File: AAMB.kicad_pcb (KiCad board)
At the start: 4 copper layers, 159.4 x 76.6 mm, 192 parts, among them J1 Screw_Terminal_01x04, J2 PJRAS4X2U01X, J3 SPKR L, J4 SPKR R, J5 Screw_Terminal_01x03, J6 Screw_Terminal_01x03, J7 Screw_Terminal_01x04, K1 G5LE-1, K2 G5LE-1, Q1 BC546, Q2 BC556, Q201 BC546, Q202 BC546, Q203 BC546, Q204 BD140, Q205 BD139, Q206 BD140, Q207 MJL21193, Q208 MJL21194, Q209 BC546, Q3 BC546, Q301 BC546, Q302 BC546, Q303 BC546, Q304 BD140, Q305 BD139, Q306 BD140, Q307 MJL21193, Q308 MJL21194, Q309 BC546, Q4 BD140, U1 TL072, U2 NE5532, U3 NE5532, U4 THAT2180, U5 DG509BEQ-T1-E3, U6 CD4071B

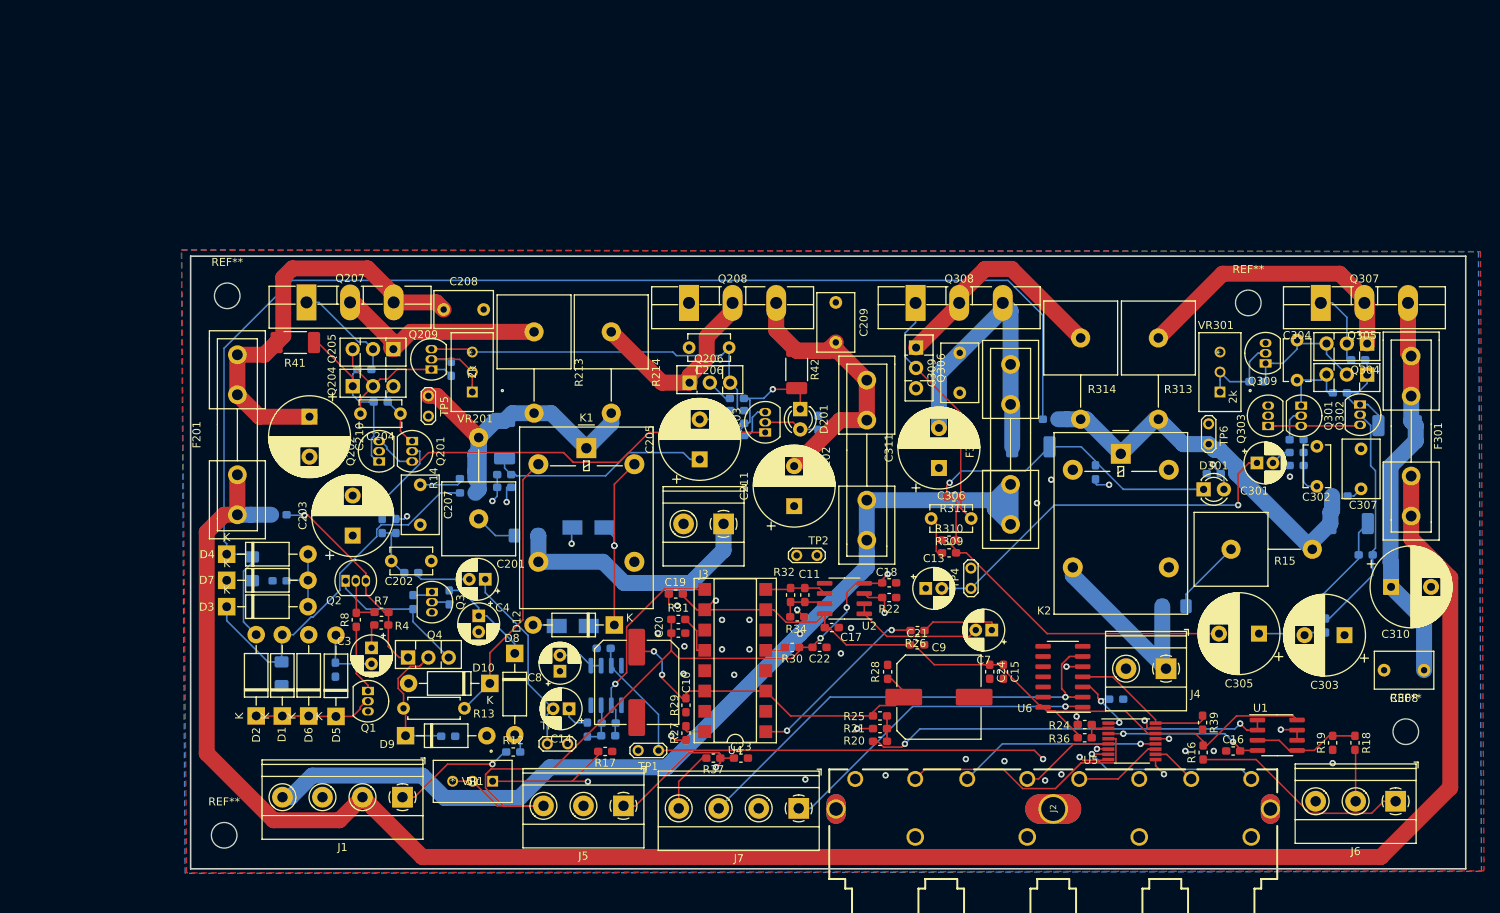
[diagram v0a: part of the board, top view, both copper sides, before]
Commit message: Lots of part changes to SMD devices. Adding MPN, MFG to all parts for BOM export.
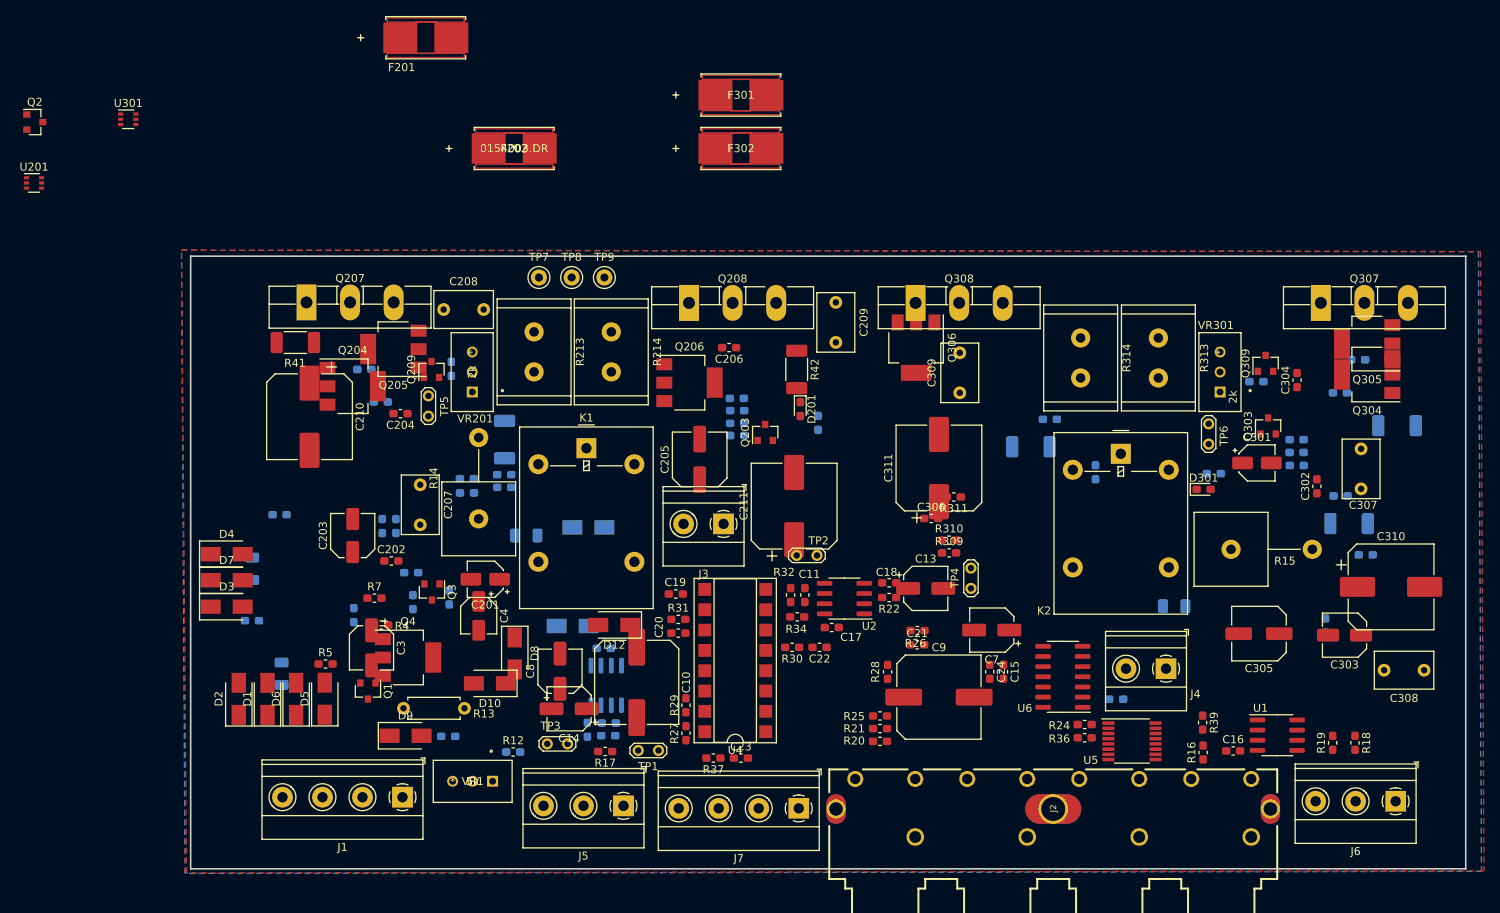
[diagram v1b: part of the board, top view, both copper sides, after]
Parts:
- removed Q201, Q202, Q301, Q302: BC546, Package_TO_SOT_THT:TO-92_Inline
- removed REF** (x4): MountingHole_3.2mm_M3, MountingHole:MountingHole_3.2mm_M3
- added TP7: 5002, digikey-footprints:Test_Point_D1.02mm, F.Cu at (102.6, 62.4)
- added TP8: 5000, digikey-footprints:Test_Point_D1.02mm, F.Cu at (106.7, 62.4)
- added TP9: 5001, digikey-footprints:Test_Point_D1.02mm, F.Cu at (110.8, 62.4)
- added U201: BC846BDW1T1G, Package_TO_SOT_SMD:SOT-363_SC-70-6, F.Cu at (39.5, 50.5)
- added U301: BC846BDW1T1G, Package_TO_SOT_SMD:SOT-363_SC-70-6, F.Cu at (51.3, 42.6)
- C1, C2, C5, C6: footprint Capacitor_SMD:C_1206_3216Metric_Pad1.42x1.75mm_HandSolder -> Capacitor_SMD:C_1206_3216Metric
- C13, C14, C3, C7, C8: footprint Capacitor_THT:CP_Radial_D5.0mm_P2.00mm -> Capacitor_SMD:CP_Elec_5x3
- C201, C301, C4: footprint Capacitor_THT:CP_Radial_D5.0mm_P2.00mm -> Capacitor_SMD:CP_Elec_4x5.4
- C202, C204, C206, C302, C304, C306: footprint Capacitor_THT:C_Disc_D5.1mm_W3.2mm_P5.00mm -> Capacitor_SMD:C_0603_1608Metric_Pad1.05x0.95mm_HandSolder
- C203, C303: footprint Capacitor_THT:CP_Radial_D10.0mm_P5.00mm -> Capacitor_SMD:C_Elec_5x5.4
- C205, C305: footprint Capacitor_THT:CP_Radial_D10.0mm_P5.00mm -> Capacitor_SMD:C_Elec_6.3x7.7
- C210, C211, C310, C311: footprint Capacitor_THT:CP_Radial_D10.0mm_P5.00mm -> Capacitor_SMD:CP_Elec_10x10.5
- D1, D10, D12, D2, D3, D4, D5, D6, D7, D8, D9: value 1N4004 -> S1G; footprint Diode_THT:D_DO-41_SOD81_P10.16mm_Horizontal -> Diode_SMD:D_SMA
- D201, D301: footprint LED_THT:LED_D3.0mm -> LED_SMD:LED_0603_1608Metric_Pad1.05x0.95mm_HandSolder
- F201, F202, F301, F302: value 3A -> 0154003.DR; footprint Fuseholders:Fuseholder5x20_horiz_open_inline_Type-I -> Fuse:0154003.DR
- J3: value SPKR L -> SPKR
- J4: value SPKR R -> SPKR
- Q1, Q203, Q209, Q3, Q303, Q309: value BC546 -> BC846; footprint Package_TO_SOT_THT:TO-92_Inline -> Package_TO_SOT_SMD:SOT-23
- Q2: value BC556 -> BC856; footprint Package_TO_SOT_THT:TO-92_Inline -> Package_TO_SOT_SMD:SOT-23
- Q204, Q206, Q304, Q306, Q4: value BD140 -> BCP53; footprint Package_TO_SOT_THT:TO-126-3_Vertical -> Package_TO_SOT_SMD:SOT-223
- Q205, Q305: value BD139 -> BCP56; footprint Package_TO_SOT_THT:TO-126-3_Vertical -> Package_TO_SOT_SMD:SOT-223
- R213, R214, R313, R314: value 15m -> 330m; footprint Resistor_THT:R_Axial_Power_L25.0mm_W9.0mm_P10.16mm_Vertical -> Resistor_THT:R_Radial_Power_L13.0mm_W9.0mm_P5.00mm
- R5: moved to F.Cu
- R8: moved to B.Cu
- TP1: value post_sw_pre_vol_L -> TP
- TP2: value post_sw_pre_vol_R -> TP
- TP3: value post_vol_pre_amp_L -> TP
- TP4: value post_vol_pre_amp_R -> TP
- TP5: value post_amp_pre_rly_L -> TP
- TP6: value post_amp_pre_rly_R -> TP
- moved F301 98.9 mm to (127.8, 39.5), turned to 0 degrees
- moved Q2 69.3 mm to (39.6, 42.9)
- moved F202 65.9 mm to (99.5, 46.2), turned to 0 degrees
- moved F201 64.1 mm to (88.4, 32.4), turned to 0 degrees
- moved F302 57.8 mm to (127.8, 46.2), turned to 0 degrees
- moved R6 6.07 mm to (66.7, 105.3), turned to 180 degrees
- moved D2 3.05 mm to (65.1, 115.0)
- moved D1 2.84 mm to (68.7, 115.0)
- moved D6 2.67 mm to (72.2, 115.0)
- moved D5 2.62 mm to (75.8, 115.0)
- moved R7 1.98 mm to (82.0, 102.4)
- moved R5 1.43 mm to (75.9, 110.7), turned to 0 degrees
- moved R8 0.66 mm to (79.5, 104.6)
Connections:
- F201 pad 1: +35V -> /audio_pwr_L/P35_fused_L
- F201 pad 2: /audio_pwr_L/P35_fused_L -> +35V
- F202 pad 1: -35V -> /audio_pwr_L/N35_fused_L
- F202 pad 2: /audio_pwr_L/N35_fused_L -> -35V
- F301 pad 1: +35V -> /audio_pwr_R/P35_fused_R
- F301 pad 2: /audio_pwr_R/P35_fused_R -> +35V
- F302 pad 1: -35V -> /audio_pwr_R/N35_fused_R
- F302 pad 2: /audio_pwr_R/N35_fused_R -> -35V
- Q4 pad 3: Net-(Q2-Pad1) -> Net-(Q2-Pad2)
- R7 pad 1: Net-(Q2-Pad2) -> Net-(Q2-Pad1)
- R8 pad 2: Net-(Q2-Pad2) -> Net-(Q2-Pad1)
- R9 pad 2: Net-(Q2-Pad1) -> Net-(Q2-Pad2)
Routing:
- net +35V: track 249.4 -> 0.00 mm
- net Net-(C2-Pad1): track 160.7 -> 0.00 mm
- net -12V: track 148.8 -> 0.00 mm, vias 5 -> 0
- net +12V: track 135.5 -> 0.00 mm, vias 2 -> 0
- net -35V: track 123.3 -> 0.00 mm, vias 1 -> 0
- net /volume/vol_pot_3: track 112.3 -> 0.00 mm, vias 1 -> 0
- net /short_protection_muting/RLY_-L_+R: track 81.1 -> 0.00 mm, vias 2 -> 0
- net /pre_vol_audio_L: track 72.3 -> 0.00 mm, vias 2 -> 0
- net Net-(C306-Pad1): track 68.4 -> 0.00 mm
- net /pre_vol_audio_R: track 61.4 -> 0.00 mm, vias 2 -> 0
- net /input_select/input_sw_3: track 59.6 -> 0.00 mm, vias 1 -> 0
- net Net-(R21-Pad2): track 59.2 -> 0.00 mm, vias 2 -> 0
- net /audio_pwr_L/P35_fused_L: track 52.4 -> 0.00 mm
- net Net-(Q203-Pad1): track 51.9 -> 0.00 mm
- net Net-(R20-Pad2): track 51.2 -> 0.00 mm, vias 2 -> 0
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
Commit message: Layout startover, sorting, some routing. Removed redundant fuses. BOM export.
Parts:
- removed F201, F202, F301, F302: 0154003.DR, Fuse:0154003.DR
- added F1: Fuse_Small, Resistor_SMD:R_1206_3216Metric_Pad1.42x1.75mm_HandSolder, F.Cu at (44.0, 182.0)
- added F2: Fuse_Small, Resistor_SMD:R_1206_3216Metric_Pad1.42x1.75mm_HandSolder, F.Cu at (34.0, 181.7)
- added TP10: 5002, digikey-footprints:Test_Point_D1.02mm, F.Cu at (379.7, 65.5)
- added TP11: 5000, digikey-footprints:Test_Point_D1.02mm, F.Cu at (383.8, 65.5)
- added TP12: 5001, digikey-footprints:Test_Point_D1.02mm, F.Cu at (387.9, 65.5)
- C1, C12, C2, C6, D11, D13, R1, R10, R11, R12, R2, R23, R3, R33, R35, R6, R8, R9, U3: moved to F.Cu
- R13: footprint Resistor_THT:R_Axial_DIN0207_L6.3mm_D2.5mm_P7.62mm_Horizontal -> Resistor_SMD:R_2512_6332Metric
- R14, R15: footprint Resistor_THT:R_Axial_Power_L25.0mm_W9.0mm_P10.16mm_Vertical -> Resistor_THT:R_Axial_DIN0918_L18.0mm_D9.0mm_P7.62mm_Vertical
- R24, R36, R39: moved to B.Cu
- moved U301 372.9 mm to (421.0, 91.5)
- moved R12 225.9 mm to (148.4, -98.8)
- moved Q4 211.2 mm to (139.7, -94.5)
- moved J3 210.9 mm to (156.7, -115.4)
- moved R6 209.9 mm to (130.2, -94.8), turned to 90 degrees
- moved D10 208.0 mm to (162.2, -84.3)
- moved K1 207.2 mm to (135.7, -121.8)
- moved C309 207.1 mm to (362.3, 78.8)
- moved Q308 207.1 mm to (356.8, 67.6)
- moved R306 207.1 mm to (409.8, 78.8)
- moved R308 207.1 mm to (394.1, 88.9)
- moved R312 207.1 mm to (412.1, 74.7)
- moved R314 207.1 mm to (377.4, 72.0)
- moved R316 207.1 mm to (399.4, 77.4)
- moved R44 207.1 mm to (417.0, 82.9)
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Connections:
- C208 pad 1: /audio_pwr_L/P35_fused_L -> +35V
- C209 pad 2: /audio_pwr_L/N35_fused_L -> -35V
- C210 pad 1: /audio_pwr_L/P35_fused_L -> +35V
- C211 pad 2: /audio_pwr_L/N35_fused_L -> -35V
- C308 pad 1: /audio_pwr_R/P35_fused_R -> +35V
- C309 pad 2: /audio_pwr_R/N35_fused_R -> -35V
- C310 pad 1: /audio_pwr_R/P35_fused_R -> +35V
- C311 pad 2: /audio_pwr_R/N35_fused_R -> -35V
- J1 pad 2: +35V -> Net-(F1-Pad1)
- J1 pad 4: -35V -> Net-(F2-Pad1)
- Q207 pad 3: /audio_pwr_L/P35_fused_L -> +35V
- Q208 pad 3: /audio_pwr_L/N35_fused_L -> -35V
- Q307 pad 3: /audio_pwr_R/P35_fused_R -> +35V
- Q308 pad 3: /audio_pwr_R/N35_fused_R -> -35V
- R41 pad 1: /audio_pwr_L/P35_fused_L -> +35V
- R42 pad 1: /audio_pwr_L/N35_fused_L -> -35V
- R44 pad 1: /audio_pwr_R/P35_fused_R -> +35V
- R45 pad 1: /audio_pwr_R/N35_fused_R -> -35V
- U4 pad 13: Net-(U4-Pad13) -> (no net)
- U4 pad 4: Net-(U4-Pad4) -> (no net)
- U6 pad 10: Net-(U6-Pad10) -> (no net)
- U6 pad 11: Net-(U6-Pad11) -> (no net)
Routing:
- net /input_select/IN4_L: track 0.00 -> 29.4 mm
- net /input_select/IN1_R: track 0.00 -> 27.4 mm
- net /input_select/IN1_L: track 0.00 -> 25.9 mm, vias 0 -> 1
- net -12V: track 0.00 -> 21.2 mm, vias 0 -> 1
- net /input_select/IN4_R: track 0.00 -> 20.6 mm
- net +12V: track 0.00 -> 19.7 mm, vias 0 -> 1
- net /input_select/input_sw_1: track 0.00 -> 16.9 mm
- net Net-(R39-Pad1): track 0.00 -> 16.1 mm, vias 0 -> 2
- net /input_select/input_sw_3: track 0.00 -> 16.0 mm
- net Net-(R38-Pad1): track 0.00 -> 15.3 mm, vias 0 -> 2
- net /input_select/IN2_R: track 0.00 -> 15.0 mm
- net /input_select/IN3_L: track 0.00 -> 14.4 mm
- net GND: track 0.00 -> 14.3 mm, vias 0 -> 15
- net /input_select/input_sw_com: track 0.00 -> 13.6 mm
- net /input_select/IN3_R: track 0.00 -> 9.74 mm
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- removed copper zone on In1.Cu, net GND
- removed copper zone on In2.Cu, net GND
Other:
- board outline removed
- copper layers 4 -> 2

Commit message: Layout progress. Added two missing decoupling caps.
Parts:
- added C25: 0.1u, Capacitor_SMD:C_0603_1608Metric_Pad1.05x0.95mm_HandSolder, F.Cu at (84.5, 257.7)
- added C26: 0.1u, Capacitor_SMD:C_0603_1608Metric_Pad1.05x0.95mm_HandSolder, B.Cu at (84.1, 270.3)
- C15, C18, C19, C21, R17, R23: moved to B.Cu
- moved C19 223.5 mm to (89.8, 262.7), turned to 270 degrees
- moved C20 217.6 mm to (85.4, 263.8), turned to 270 degrees
- moved C22 212.9 mm to (97.7, 263.7), turned to 270 degrees
- moved C9 173.2 mm to (104.2, 275.8)
- moved C7 167.0 mm to (103.3, 266.5)
- moved C15 166.2 mm to (80.4, 283.7), turned to 90 degrees
- moved C21 162.8 mm to (93.4, 262.7), turned to 270 degrees
- moved R28 162.8 mm to (97.9, 272.7)
- moved C8 162.6 mm to (81.5, 273.6), turned to 90 degrees
- moved U1 162.0 mm to (81.0, 283.8), turned to 180 degrees
- moved R26 160.2 mm to (98.7, 269.6)
- moved C13 159.3 mm to (110.2, 266.3), turned to 270 degrees
- moved R25 158.9 mm to (75.4, 281.6), turned to 0 degrees
- moved R20 158.8 mm to (75.4, 283.1), turned to 0 degrees
- moved R21 158.8 mm to (75.5, 284.7), turned to 0 degrees
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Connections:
- net Net-(R27-Pad2) renamed /volume/vca_in_L
- U3 pad 4: (no net) -> -12V
- U3 pad 8: (no net) -> +12V
- U4 pad 13: (no net) -> Net-(U4-Pad13)
- U4 pad 4: (no net) -> Net-(U4-Pad4)
- U6 pad 10: (no net) -> Net-(U6-Pad10)
- U6 pad 11: (no net) -> Net-(U6-Pad11)
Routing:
- net +12V: track 19.7 -> 98.1 mm, vias 1 -> 3
- net -12V: track 21.2 -> 91.8 mm, vias 1 -> 4
- net /pre_vol_audio_L: track 1.47 -> 70.1 mm, vias 1 -> 2
- net /pre_vol_audio_R: track 0.00 -> 63.2 mm
- net /volume/v_ec-: track 0.00 -> 38.2 mm
- net /volume/vol_pot_2: track 0.00 -> 29.3 mm, vias 0 -> 1
- net GND: track 14.3 -> 40.9 mm, vias 15 -> 39
- net /volume/vol_pot_1: track 0.00 -> 26.3 mm, vias 0 -> 1
- net /volume/vca_in_R: track 0.00 -> 16.4 mm
- net /volume/vol_pot_3: track 0.00 -> 14.8 mm
- net Net-(C13-Pad1): track 0.00 -> 11.4 mm
- net Net-(C11-Pad1): track 0.00 -> 9.96 mm
- net Net-(R20-Pad2): track 0.00 -> 9.43 mm
- net Net-(R18-Pad1): track 0.00 -> 9.23 mm
- net Net-(C7-Pad2): track 0.00 -> 8.33 mm
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
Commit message: Capturing layout progress.
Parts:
- removed C201, C301: 4.7u, Capacitor_SMD:CP_Elec_4x5.4
- removed TP10, TP7: 5002, digikey-footprints:Test_Point_D1.02mm
- removed TP11, TP8: 5000, digikey-footprints:Test_Point_D1.02mm
- removed TP12, TP9: 5001, digikey-footprints:Test_Point_D1.02mm
- C302, C6, R311, R41, U301: moved to B.Cu
- R201, R202, R203, R204, R205, R207, R208, R209, R210, R211, R308, R40: moved to F.Cu
- moved C2 331.4 mm to (111.8, 246.8), turned to 0 degrees
- moved C3 331.0 mm to (104.9, 242.1), turned to 0 degrees
- moved Q307 331.0 mm to (115.6, 223.6)
- moved R3 326.6 mm to (100.2, 240.2)
- moved D5 323.0 mm to (103.8, 248.6)
- moved R2 322.5 mm to (111.1, 244.7)
- moved R4 321.4 mm to (100.2, 244.0), turned to 180 degrees
- moved D6 319.1 mm to (105.5, 254.0), turned to 180 degrees
- moved C309 316.3 mm to (92.8, 244.5)
- moved D2 314.8 mm to (111.1, 251.5)
- moved D1 313.1 mm to (107.4, 248.6)
- moved Q305 312.5 mm to (181.1, 259.4), turned to 90 degrees
- moved R43 305.2 mm to (160.8, 270.0), turned to 90 degrees
- moved Q308 304.9 mm to (94.9, 223.6)
- moved Q303 299.9 mm to (168.0, 272.0)
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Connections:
- net Net-(F1-Pad1) renamed /+35V_UNFUSED
- net Net-(F2-Pad1) renamed /-35V_UNFUSED
- R201 pad 2: Net-(C201-Pad2) -> /line_audio_L
- R301 pad 2: Net-(C301-Pad2) -> /line_audio_R

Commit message: Place and route complete. Silkscreen cleanup needed.
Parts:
- C15, C18, C19, C21, C26, C302, C5, C6, R17, R206, R212, R215, R216, R23, R24, R301, R302, R303, R304, R305, R306, R307, R311, R312, R315, R316, R36, R38, R39, R41, R43, R44, R45, U301: moved to F.Cu
- VR1: footprint Murata-POT:PV36W202C01B00 -> Potentiometer_THT:Nidec_CT6EP202
- VR201, VR301: footprint Murata-POT:PV36W202C01B00 -> Potentiometer_THT:Potentiometer_Bourns_3296W_Vertical
- moved C210 305.1 mm to (163.8, 73.7)
- moved C208 285.4 mm to (174.5, 71.4)
- moved Q209 252.4 mm to (101.9, 62.7), turned to 0 degrees
- moved R216 249.0 mm to (98.0, 62.7), turned to 270 degrees
- moved C204 237.2 mm to (79.5, 75.8), turned to 90 degrees
- moved C303 233.3 mm to (154.3, 75.8), turned to 0 degrees
- moved C207 227.1 mm to (87.2, 98.6), turned to 90 degrees
- moved R304 223.4 mm to (171.0, 81.7), turned to 180 degrees
- moved R215 221.2 mm to (88.4, 101.9), turned to 90 degrees
- moved C203 220.9 mm to (94.1, 53.0), turned to 270 degrees
- moved TP5 212.6 mm to (88.4, 105.1)
- moved Q306 211.2 mm to (160.5, 61.2)
- moved Q304 209.7 mm to (180.7, 77.8), turned to 0 degrees
- moved C308 208.4 mm to (203.3, 57.8)
- moved C209 207.5 mm to (176.1, 56.8)
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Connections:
- J1 pad 1: 25Vac -> /+35V_UNFUSED
- J1 pad 2: /+35V_UNFUSED -> GND
- J1 pad 3: GND -> /-35V_UNFUSED
- J1 pad 4: /-35V_UNFUSED -> 25Vac
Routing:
- net +35V: track 0.00 -> 213.7 mm, vias 0 -> 2
- net /pwr_audio_R: track 0.00 -> 158.8 mm, vias 0 -> 1
- net -35V: track 0.00 -> 145.6 mm, vias 0 -> 1
- net /short_protection_muting/RLY_-L_+R: track 0.00 -> 140.9 mm, vias 0 -> 1
- net /pwr_audio_L: track 0.00 -> 100.8 mm, vias 0 -> 1
- net Net-(C204-Pad2): track 0.00 -> 68.5 mm, vias 0 -> 4
- net Net-(C306-Pad1): track 0.00 -> 67.2 mm, vias 0 -> 3
- net Net-(Q205-Pad2): track 0.00 -> 59.2 mm, vias 0 -> 1
- net Net-(C306-Pad2): track 0.00 -> 56.5 mm, vias 0 -> 2
- net +12V: track 98.1 -> 154.0 mm, vias 3 -> 0
- net /line_audio_L: track 0.00 -> 51.4 mm
- net Net-(C304-Pad2): track 0.00 -> 51.0 mm
- net /pre_vol_audio_L: track 70.1 -> 25.1 mm, vias 2 -> 0
- net /short_protection_muting/audio_rly_out_L: track 0.00 -> 44.2 mm
- net /short_protection_muting/RLY_+L: track 0.00 -> 43.9 mm
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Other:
- board outline added: 148.7 x 80.4 mm
- net class VCC_audio added: clearance 0.1, trace_width 0.4, via_dia 0.8, via_drill 0.4
